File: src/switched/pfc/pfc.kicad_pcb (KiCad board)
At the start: 2 copper layers, 100 x 90.8 mm, 68 parts, among them J1 AC-input, J2 Conn_01x02, J3 Conn_01x02, Q1 AOT190A60CL‎, U1 AP3917B, U2 bd7692fj

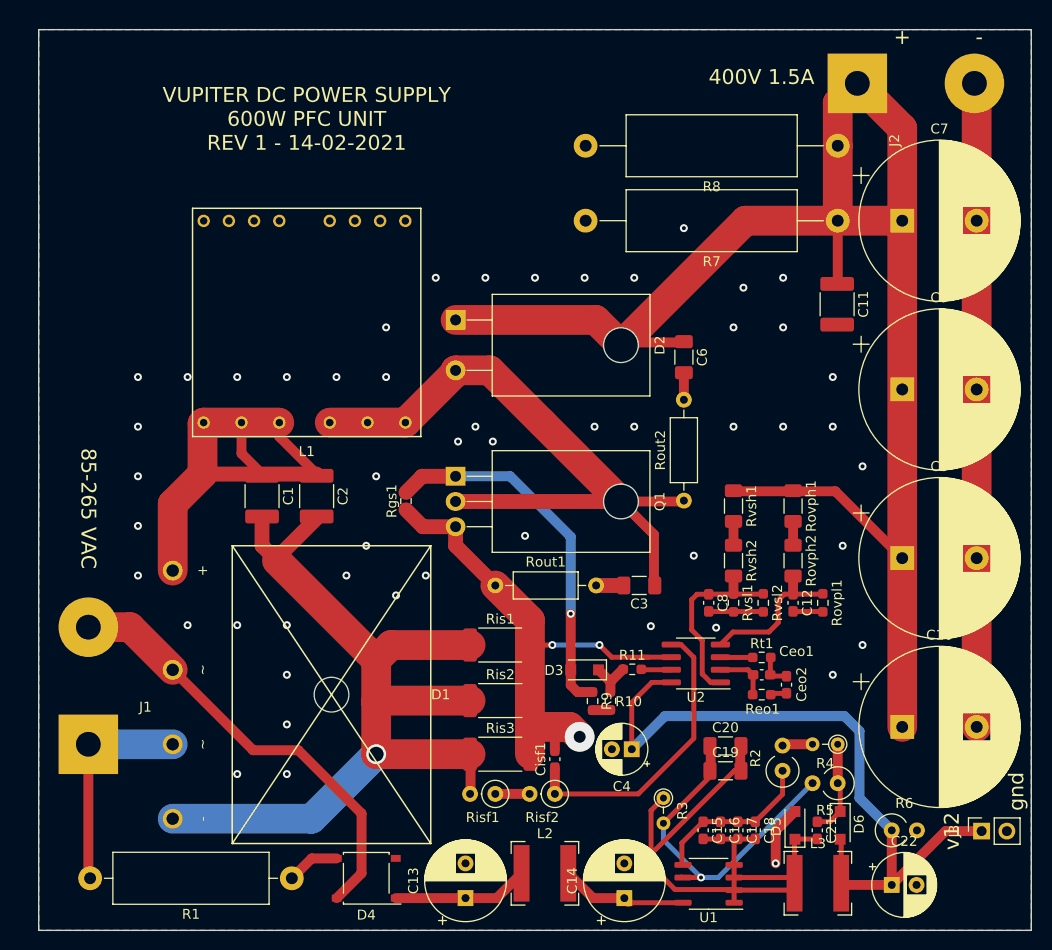
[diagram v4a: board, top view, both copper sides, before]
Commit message: Low effort input filter added to pfc, vestigial input port remains for potential issues
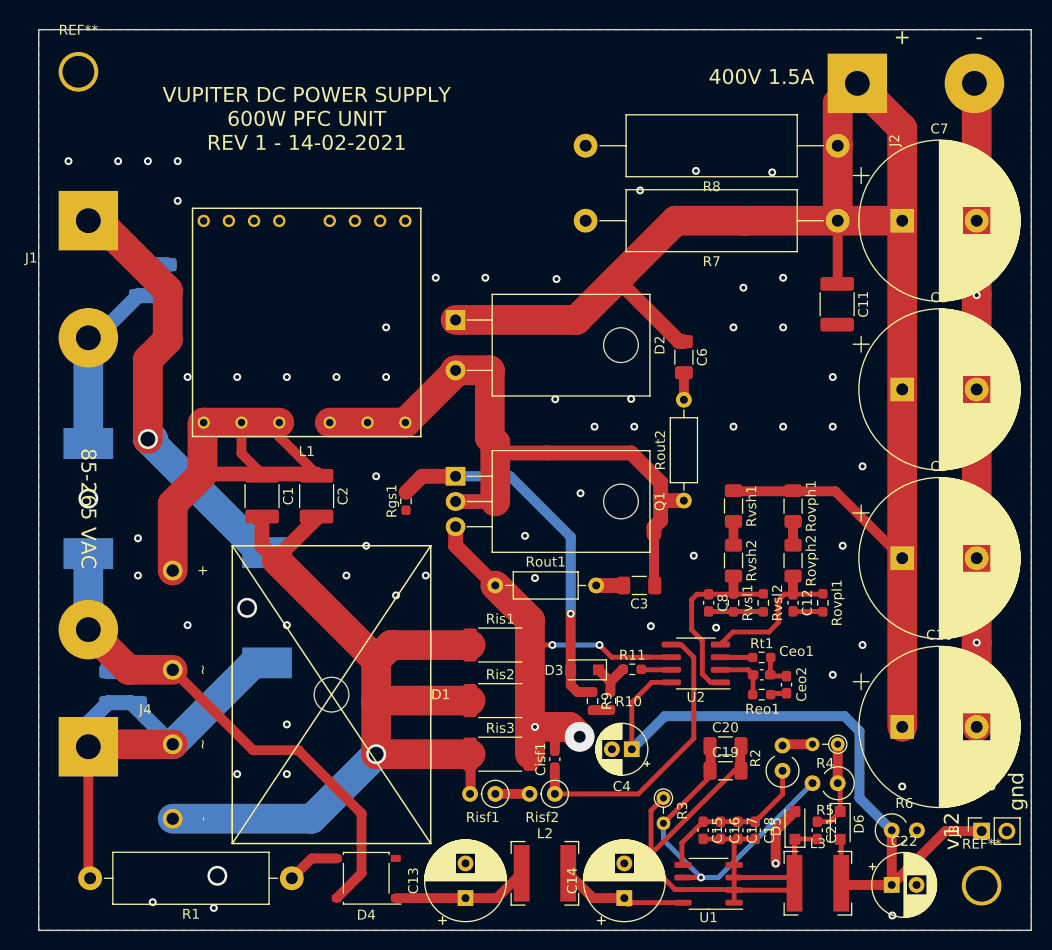
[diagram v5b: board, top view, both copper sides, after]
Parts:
- added C23: 100n, Capacitor_SMD:C_1206_3216Metric_Pad1.33x1.80mm_HandSolder, B.Cu at (110.0, 75.2)
- added C24: 100n, Capacitor_SMD:C_1206_3216Metric_Pad1.33x1.80mm_HandSolder, B.Cu at (113.0, 75.2)
- added C25: 100n, Capacitor_SMD:C_1206_3216Metric_Pad1.33x1.80mm_HandSolder, B.Cu at (110.0, 116.2)
- added C26: 100n, Capacitor_SMD:C_1206_3216Metric_Pad1.33x1.80mm_HandSolder, B.Cu at (107.0, 116.2)
- added J4: AC-input, custom:spacedConnector, F.Cu at (105.0, 122.2)
- added L4: 22u, custom:TMPC1206HP, B.Cu at (123.0, 108.2)
- added L5: 22u, custom:TMPC1206HP, B.Cu at (105.0, 97.2)
- added REF**: MountingHole_3.2mm_M3, MountingHole:MountingHole_3.2mm_M3, F.Cu at (195.0, 136.2)
- added REF**: MountingHole_3.2mm_M3, MountingHole:MountingHole_3.2mm_M3, F.Cu at (104.0, 54.2)
- moved J1 52.8 mm to (105.0, 69.2), turned to 270 degrees
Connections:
- J1 pad 1: v120p -> Net-(C23-Pad1)
- J1 pad 2: v120n -> Net-(C23-Pad2)
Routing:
- net Net-(C23-Pad1): track 0.00 -> 53.9 mm, vias 0 -> 1
- net v120p: track 22.1 -> 48.6 mm
- net Net-(C23-Pad2): track 0.00 -> 20.4 mm
- net v120n: track 44.9 -> 64.1 mm
- net gnd: track 138.0 -> 132.3 mm, vias 54 -> 66
- net Net-(C3-Pad1): track 70.0 -> 67.4 mm
- net vpfc: track 166.5 -> 165.9 mm
- net (no net): vias 0 -> 1

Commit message: final boards and initial blinky
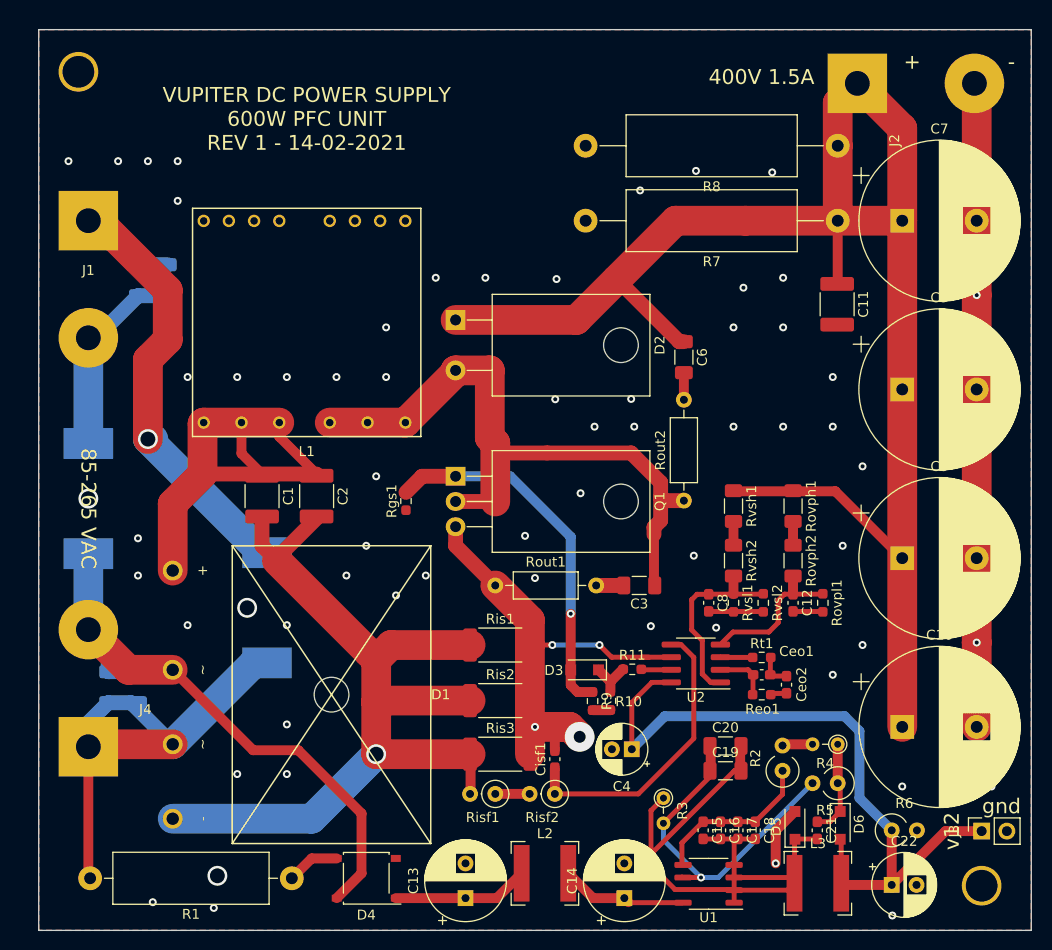
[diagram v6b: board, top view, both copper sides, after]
